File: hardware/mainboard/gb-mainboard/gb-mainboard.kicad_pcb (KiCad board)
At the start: 2 copper layers, 77.4 x 81 mm, 55 parts, among them P101 NUCLEO-CN7, P102 NUCLEO-CN10, P103 MOTOR_SX, P104 MOTOR_DX, P105 WE-632723300011, P106 BATTERY, P107 EN_JMP, P108 BOOT_JMP, P109 ESP_PROG, Q101 DMP2120U-7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

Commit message: Added address jumper.
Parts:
- added G***: LOGO, EXTLOGO:GIAMMABOT_35MM_FSILK, F.Cu at (126.1, 88.9)
- added J101: JUMPER-2_1, MISC:JUMPERSMD-2-0805, F.Cu at (103.2, 85.9)
- added J102: JUMPER-2_1, MISC:JUMPERSMD-2-0805, F.Cu at (103.2, 83.8)
- added J103: JUMPER-2_1, MISC:JUMPERSMD-2-0805, F.Cu at (103.2, 81.7)
- moved D102 0.47 mm to (146.1, 104.9), turned to 270 degrees
- moved D101 0.37 mm to (146.5, 122.4), turned to 180 degrees
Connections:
- D101 pad 1: GND -> +VUSB
- D101 pad 2: +VUSB -> GND
- D102 pad 1: +VUSB -> Net-(D102-Pad1)
- D102 pad 2: Net-(D102-Pad2) -> +VUSB
- P102 pad 26: Net-(P102-Pad26) -> /ADDR_0
- P102 pad 28: Net-(P102-Pad28) -> /ADDR_1
- P102 pad 30: Net-(P102-Pad30) -> /ADDR_2
- P102 pad 32: Net-(P102-Pad32) -> GND
- Q101 pad 2: Net-(D102-Pad2) -> Net-(D102-Pad1)
- SW101 pad 3: Net-(D102-Pad2) -> Net-(D102-Pad1)
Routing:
- net Net-(D102-Pad2): track 33.0 -> 0.00 mm
- net Net-(D102-Pad1): track 0.00 -> 33.0 mm
- net GND: track 78.9 -> 109.6 mm, vias 19 -> 25
- net /ADDR_0: track 0.00 -> 6.10 mm
- net /ADDR_1: track 0.00 -> 5.94 mm
- net /ADDR_2: track 0.00 -> 5.90 mm
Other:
- board text added: "OFF"
- board text added: "ON"

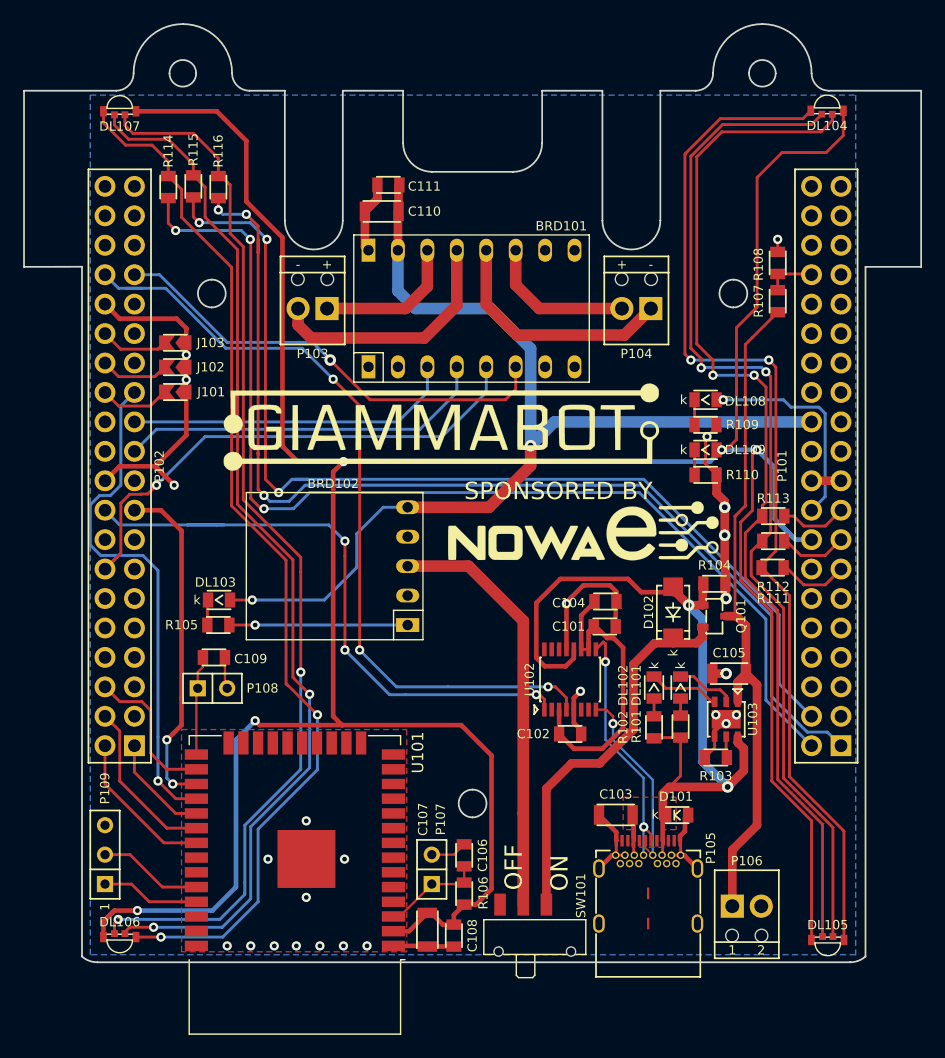
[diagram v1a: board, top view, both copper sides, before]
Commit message: Fixed silkscreen main board
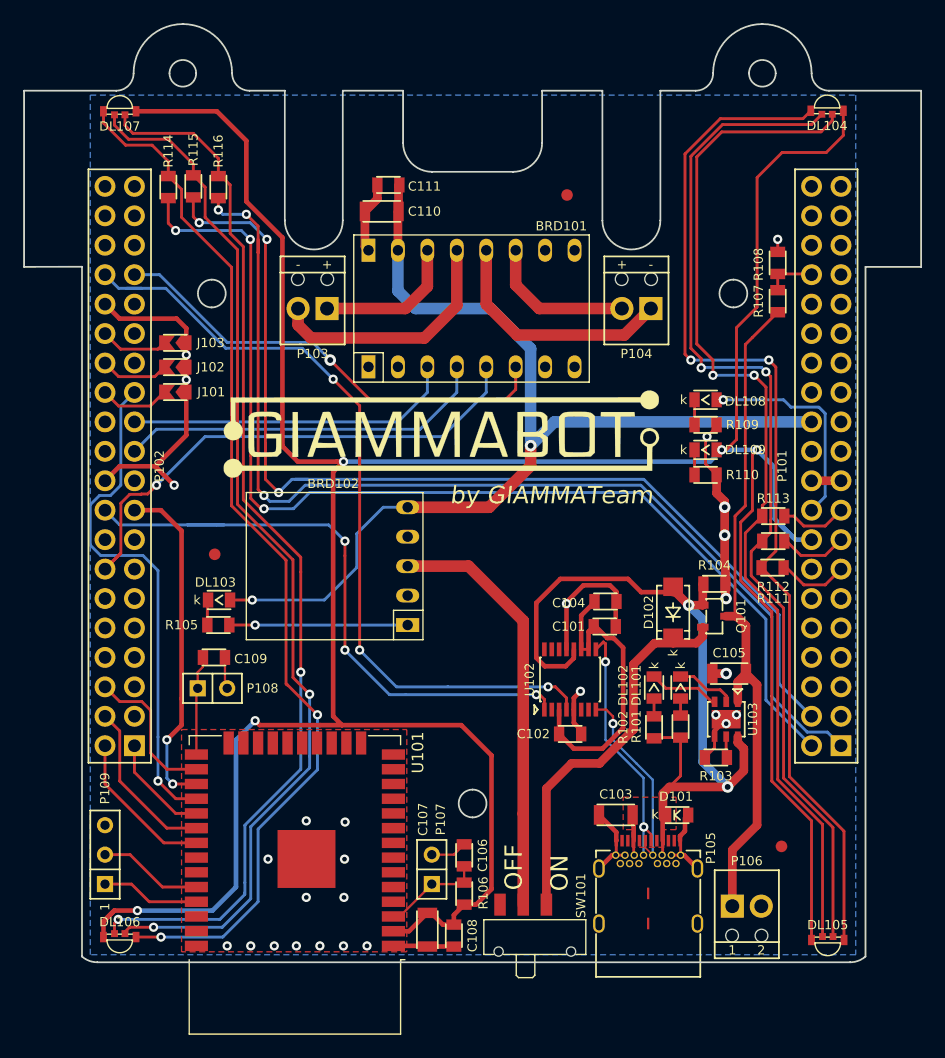
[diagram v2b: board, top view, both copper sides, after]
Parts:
- removed the G*** at (138.4, 97.9)
- added G***: LOGO, LOGO:LOGO_NOWAE_30MM_FSILK, B.Cu at (139.6, 106.1)
- added G***: LOGO, EXTLOGO:LOGO_CC-BY-SA_20MM_FSILK, B.Cu at (112.9, 116.6)
- added G***: LOGO, EXTLOGO:LOGO_OSH_10MM_FSILK, B.Cu at (113.1, 103.5)
- added G***: LOGO, EXTLOGO:GIAMMABOT_35MM_FSILK, B.Cu at (126.0, 88.8)
- added VAL**: FIDUCIALMARK_1MM_3MM, MECHANICAL:FIDUCIALMARK_1MM_3MM, F.Cu at (106.6, 99.9)
- added VAL**: FIDUCIALMARK_1MM_3MM, MECHANICAL:FIDUCIALMARK_1MM_3MM, F.Cu at (155.5, 125.1)
- added VAL**: FIDUCIALMARK_1MM_3MM, MECHANICAL:FIDUCIALMARK_1MM_3MM, F.Cu at (137.0, 68.9)
- moved G*** 0.60 mm to (126.1, 89.5)
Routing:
- net GND: vias 25 -> 27
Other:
- board text added: "GB-MAINBOARD Rev. 0"
- board text added: "by GIAMMATeam"
